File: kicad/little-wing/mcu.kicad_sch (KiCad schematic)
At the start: 25 parts, among them X1 ${ALTIUM_VALUE}, X2 ${ALTIUM_VALUE}

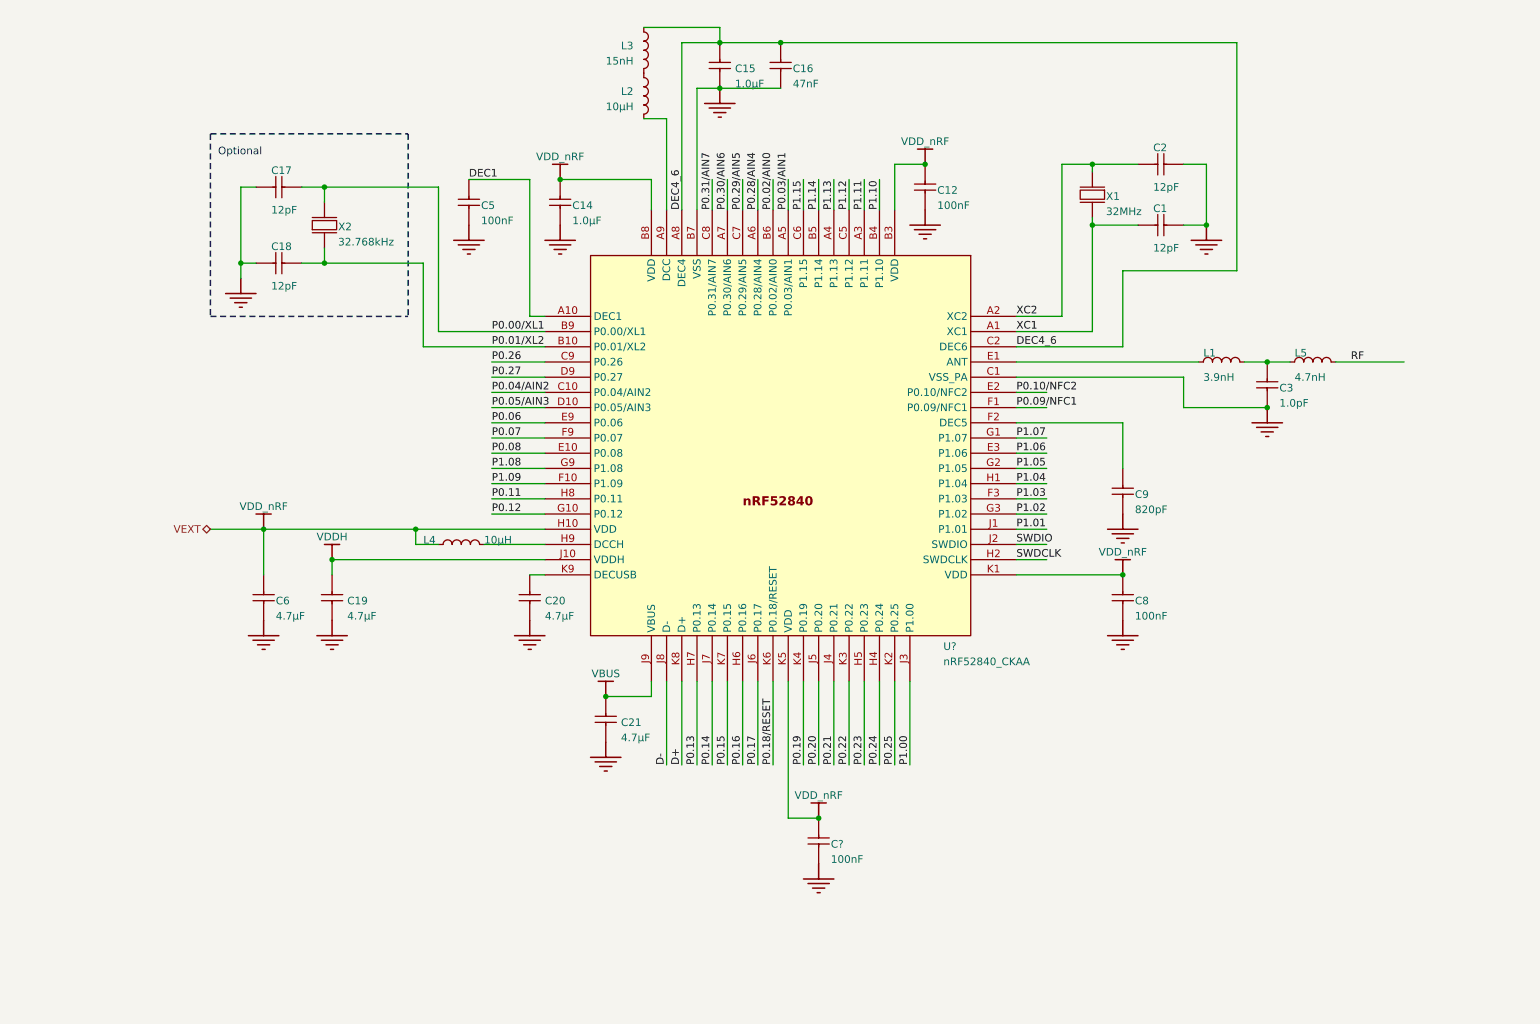
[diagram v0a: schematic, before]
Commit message: Re-shuffling the schematics across sub-sheets
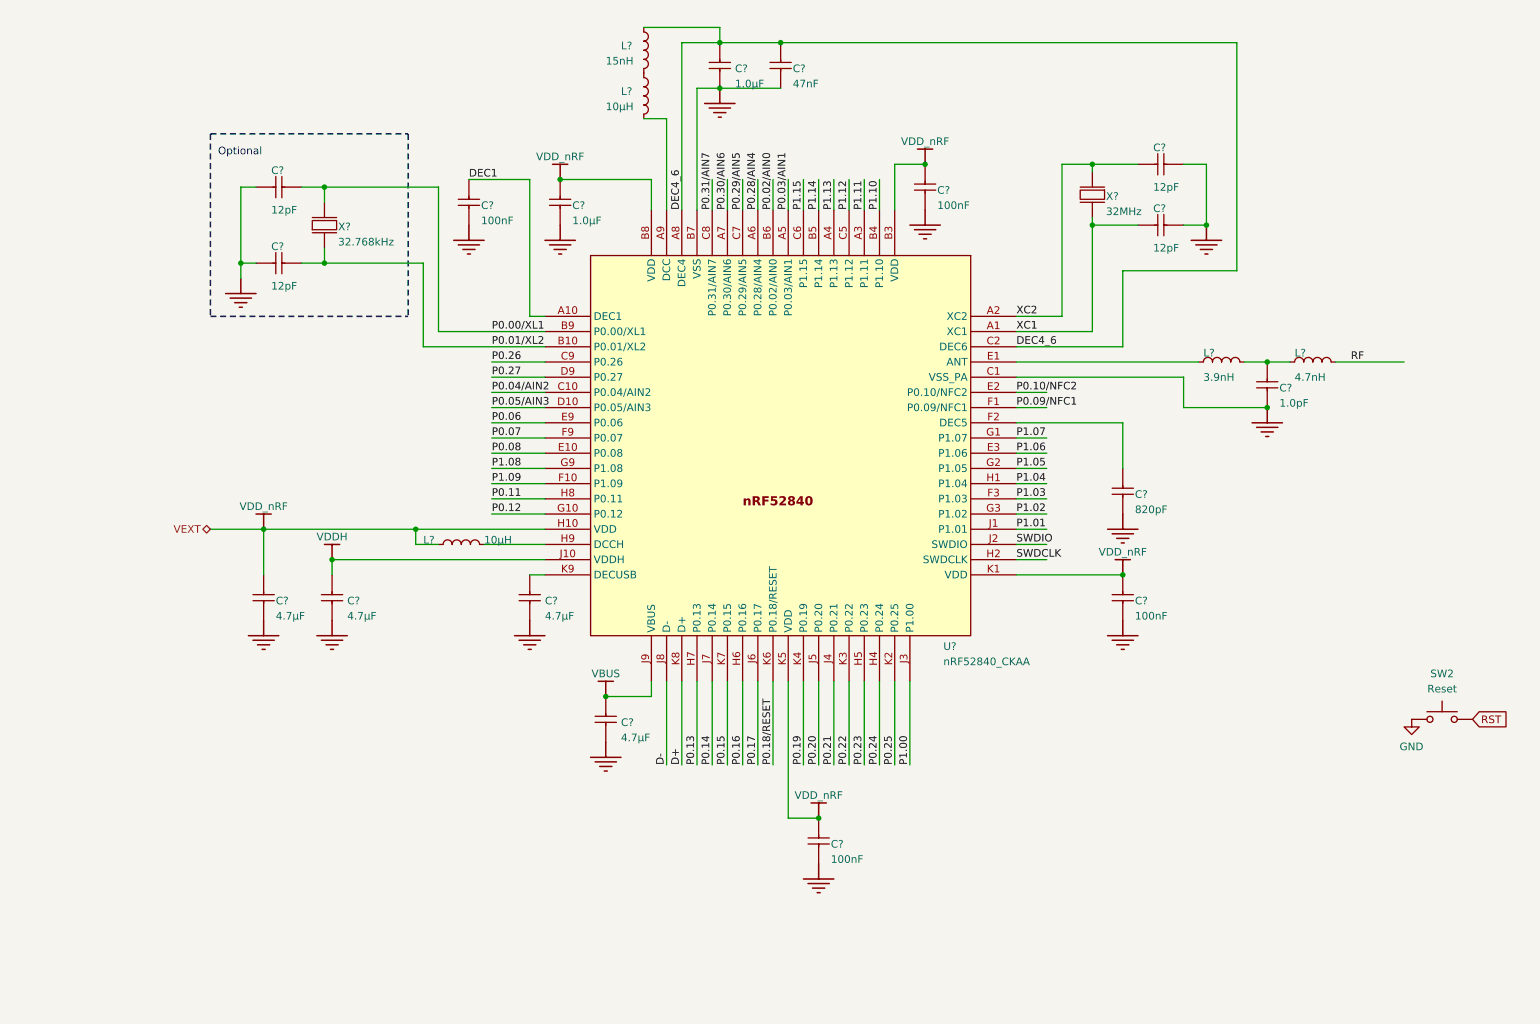
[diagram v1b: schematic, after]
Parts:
- added SW2: Reset, Button_Switch_SMD:SW_SPST_B3U-1000P, symbol ScottoKeebs:Placeholder_Switch
- renumbered C3 to C?, C9 to C?, C6 to C?, C12 to C?, C2 to C?, C16 to C?, C15 to C?, C19 to C?, C21 to C?, C20 to C?, C18 to C?, C1 to C?, C17 to C?, C14 to C?, C5 to C?, C8 to C?, L3 to L?, L5 to L?, L1 to L?, L2 to L?, L4 to L?, X2 to X?, X1 to X?
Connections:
- net GND: now also SW2.1
- new net RST: SW2.2

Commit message: Tidying up the mess a little bit
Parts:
- gave numbers to parts that had none: 25
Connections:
- net P0.18/RESET is gone; now on net RST: U1.K6 (P0.18/RESET)
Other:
- note removed: "Optional"

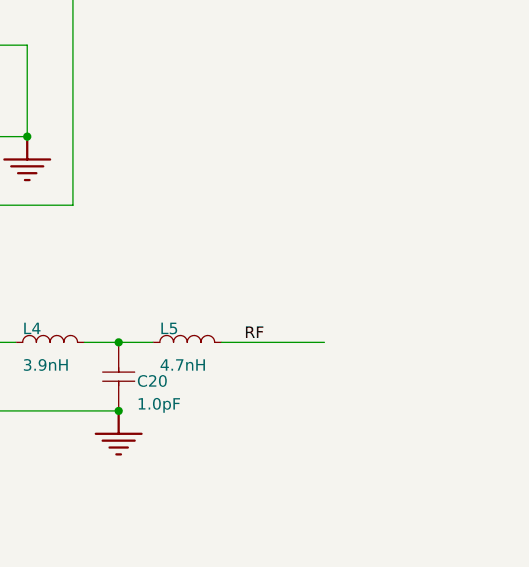
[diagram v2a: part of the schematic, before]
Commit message: Re-importing some key components
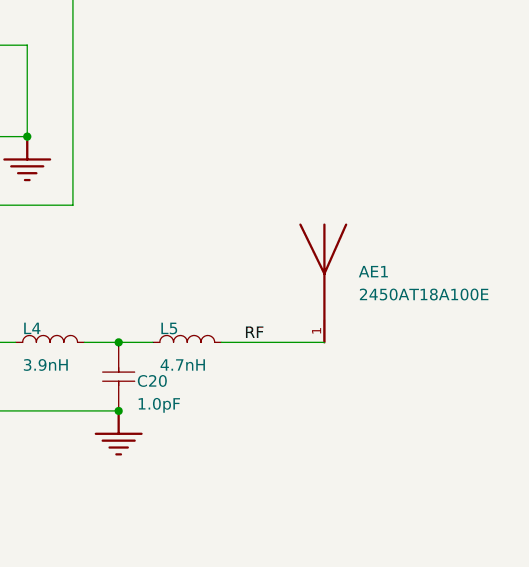
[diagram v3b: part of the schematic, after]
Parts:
- added AE1: 2450AT18A100E, JTI Antenna:ANTC3216X140N, symbol JTI Antenna:2450AT18A100E
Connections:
- net RF: now also AE1.1
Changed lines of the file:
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@@
+	)
+	(symbol
+		(lib_id "JTI Antenna:2450AT18A100E")
+		(at 255.27 74.93 0)
+		(unit 1)
+		(exclude_from_sim no)
+		(in_bom yes)
+		(on_board yes)
+		(dnp no)
+		(fields_autoplaced yes)
+		(property "Reference" "AE1"
+			(at 259.08 72.1994 0)
+			(effects
+				(font
+					(size 1.27 1.27)
+				)
+				(justify left)
+			)
+		)
+		(property "Value" "2450AT18A100E"
+			(at 259.08 74.7394 0)
+			(effects
+				(font
+					(size 1.27 1.27)
+				)
+				(justify left)
+			)
+		)
+		(property "Footprint" "JTI Antenna:ANTC3216X140N"
+			(at 255.27 74.93 0)
+			(effects
+				(font
+					(size 1.27 1.27)
+				)
+				(justify bottom)
+				(hide yes)
+			)
+		)
+		(property "Datasheet" ""
+			(at 255.27 74.93 0)
+			(effects
+				(font
+					(size 1.27 1.27)
+				)
+				(hide yes)
+			)
+		)
+		(property "Description" ""
+			(at 255.27 74.93 0)
+			(effects
+				(font
+					(size 1.27 1.27)
+				)
+				(hide yes)
+			)
+		)
+		(property "MF" "Johanson Technology"
+			(at 255.27 74.93 0)
+			(effects
+				(font
+					(size 1.27 1.27)
+				)
+				(justify bottom)
+				(hide yes)
+			)
+		)
+		(property "Description_1" "2.4GHz - Chip RF Antenna 2.4GHz ~ 2.5GHz 0.5dBi Solder Surface Mount"
+			(at 255.27 74.93 0)
+			(effects
+				(font
+					(size 1.27 1.27)
+				)
+				(justify bottom)
+				(hide yes)
+			)
+		)
+		(property "Package" "Package"
+			(at 255.27 74.93 0)
+			(effects
+				(font
+					(size 1.27 1.27)
+				)
+				(justify bottom)
+				(hide yes)
+			)
+		)
+		(property "Price" "None"
+			(at 255.27 74.93 0)
+			(effects
+				(font
+					(size 1.27 1.27)
+				)
+				(justify bottom)
+				(hide yes)
+			)
+		)
+		(property "Check_prices" "https://www.snapeda.com/parts/2450AT18A100E/Johanson/view-part/?ref=eda"
+			(at 255.27 74.93 0)
+			(effects
+				(font
+					(size 1.27 1.27)
+				)
+				(justify bottom)
+				(hide yes)
+			)
+		)
+		(property "STANDARD" "IPC-7351B"
+			(at 255.27 74.93 0)
+			(effects
+				(font
+					(size 1.27 1.27)
+				)
+				(justify bottom)
+				(hide yes)
+			)
+		)
+		(property "PARTREV" "1.3"
+			(at 255.27 74.93 0)
+			(effects
+				(font
+					(size 1.27 1.27)
+				)
+				(justify bottom)
+				(hide yes)
+			)
+		)
+		(property "SnapEDA_Link" "https://www.snapeda.com/parts/2450AT18A100E/Johanson/view-part/?ref=snap"
+			(at 255.27 74.93 0)
+			(effects
+				(font
+					(size 1.27 1.27)
+				)
+				(justify bottom)
+				(hide yes)
+			)
+		)
+		(property "MP" "2450AT18A100E"
+			(at 255.27 74.93 0)
+			(effects
+				(font
+					(size 1.27 1.27)
+				)
+				(justify bottom)
+				(hide yes)
+			)
+		)
+		(property "Availability" "In Stock"
+			(at 255.27 74.93 0)
+			(effects
+				(font
+					(size 1.27 1.27)
+				)
+				(justify bottom)
+				(hide yes)
+			)
+		)
+		(property "MANUFACTURER" "JOHANSON DESIGN"
+			(at 255.27 74.93 0)
+			(effects
+				(font
+					(size 1.27 1.27)
+				)
+				(justify bottom)
+				(hide yes)
+			)
+		)
+		(pin "1"
+		)
+		(instances
+			(project ""
+				(path "/3a835e6f-a660-4b38-a102-87841cdd95ed/eaaf4618-ba3d-41b4-8a99-4f719e243661/ebcf195d-f1fd-431a-a78e-86a1a85cb647"
+					(reference "AE1")
+					(unit 1)
+				)
+			)
+		)
 	)
 	(symbol

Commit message: Adding the antennae
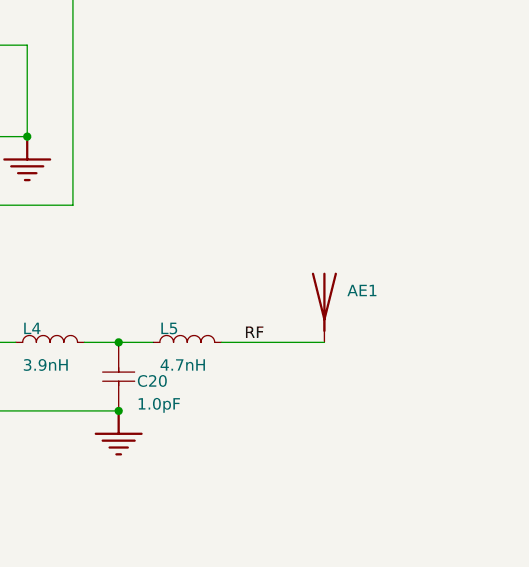
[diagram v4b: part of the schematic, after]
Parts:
- AE1: symbol JTI Antenna:2450AT18A100E -> Device:Antenna
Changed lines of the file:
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@@
 	)
 	(symbol
-		(lib_id "JTI Antenna:2450AT18A100E")
+		(lib_id "Device:Antenna")
 		(at 255.27 74.93 0)
 		(unit 1)
@@
 		(fields_autoplaced yes)
 		(property "Reference" "AE1"
-			(at 259.08 72.1994 0)
+			(at 257.81 74.2949 0)
 			(effects
 				(font
@@
 		)
 		(property "Value" "2450AT18A100E"
-			(at 259.08 74.7394 0)
+			(at 257.81 76.8349 0)
 			(effects
 				(font
@@
 				)
 				(justify left)
+				(hide yes)
 			)
 		)
@@
 					(size 1.27 1.27)
 				)
-				(justify bottom)
 				(hide yes)
 			)
 		)
-		(property "Datasheet" ""
+		(property "Datasheet" "~"
 			(at 255.27 74.93 0)
 			(effects
@@
 			)
 		)
-		(property "Description" ""
+		(property "Description" "Antenna"
 			(at 255.27 74.93 0)
 			(effects

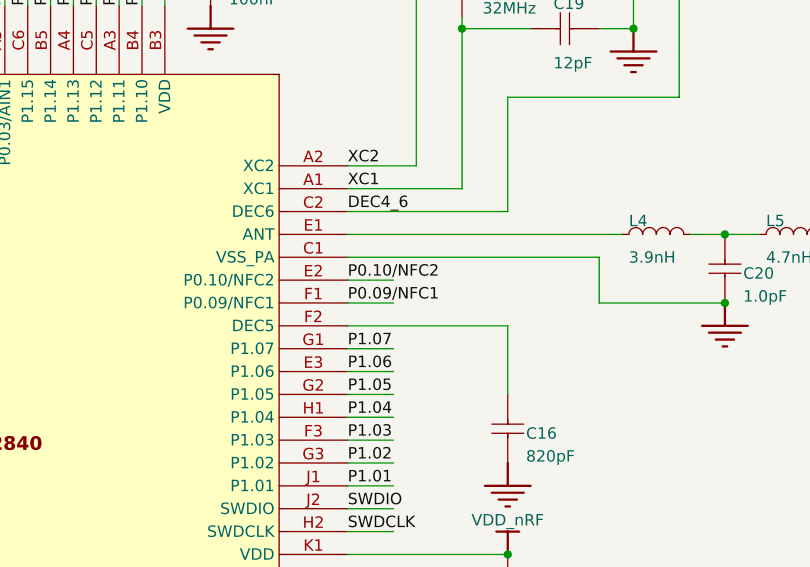
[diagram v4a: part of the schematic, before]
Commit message: Removing the NFC1/2 connectors
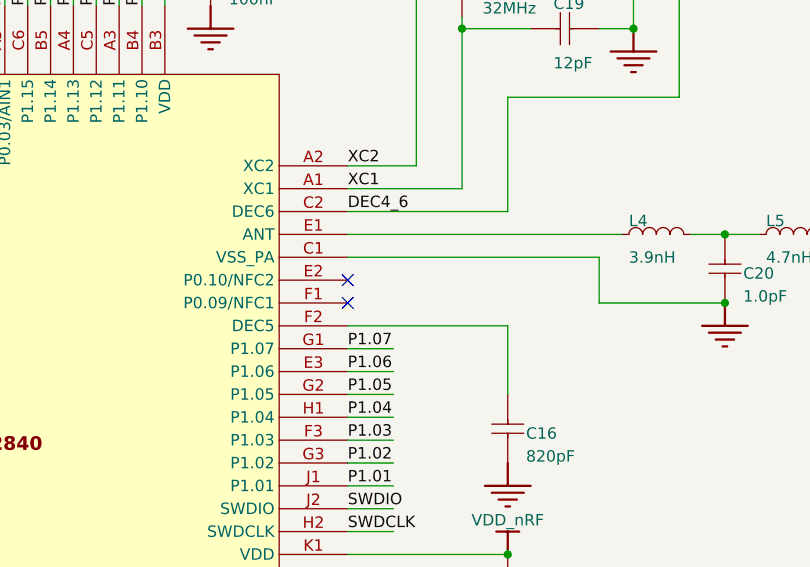
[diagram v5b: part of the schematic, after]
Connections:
- net P0.09/NFC1: no longer names the net of U1.F1 (P0.09/NFC1)
- net P0.10/NFC2: no longer names the net of U1.E2 (P0.10/NFC2)
- no-connect marks 0 -> 2
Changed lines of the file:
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@@
 		(color 0 0 0 0)
 	)
+	(no_connect
+		(at 190.5 85.09)
+	)
+	(no_connect
+		(at 190.5 87.63)
+	)
 	(wire
 		(pts
@@
 	(wire
 		(pts
-			(xy 190.5 87.63) (xy 195.58 87.63)
-		)
-		(stroke
-			(width 0)
-			(type default)
-		)
-	)
-	(wire
-		(pts
 			(xy 137.16 147.32) (xy 137.16 133.35)
 		)
@@
 		(pts
 			(xy 91.44 63.5) (xy 91.44 77.47)
-		)
-		(stroke
-			(width 0)
-			(type default)
-		)
-	)
-	(wire
-		(pts
-			(xy 190.5 85.09) (xy 195.58 85.09)
 		)
 		(stroke
@@
 		)
 	)
-	(label "P0.10/NFC2"
-		(at 190.5 85.09 0)
-		(effects
-			(font
-				(size 1.27 1.27)
-			)
-			(justify left bottom)
-		)
-	)
 	(label "DEC4_6"
 		(at 190.5 77.47 0)
@@
 		(effects
 			(font
-				(size 1.27 1.27)
-			)
-			(justify left bottom)
-		)
-	)
-	(label "P0.09/NFC1"
-		(at 190.5 87.63 0)
-		(effects
-			(font
